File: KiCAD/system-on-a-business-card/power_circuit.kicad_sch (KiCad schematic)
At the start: 12 parts, among them U4 ZD1117ILTRAD

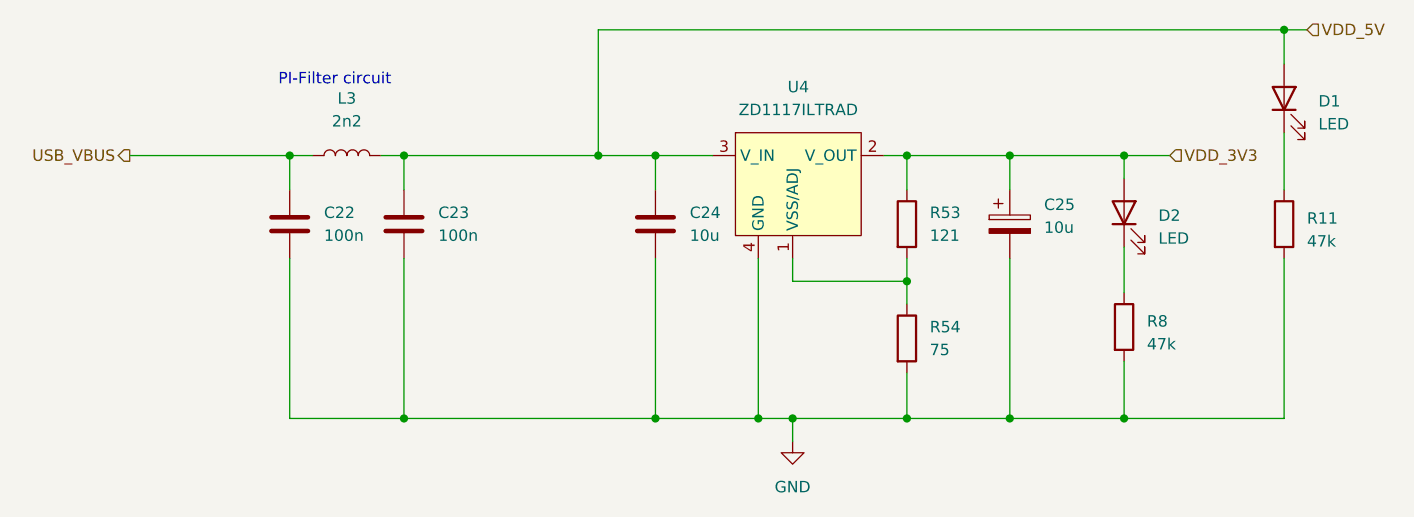
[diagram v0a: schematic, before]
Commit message: #10: mintor tweaks in routing, removed fiducials from bom, added values to buzzer and sd-card slot
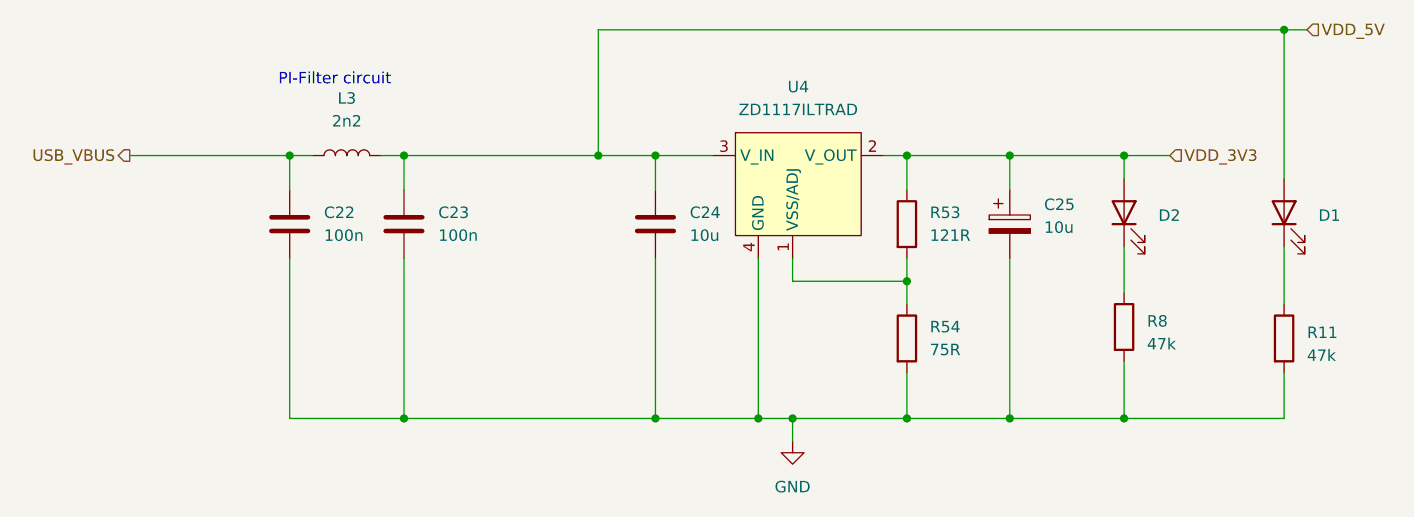
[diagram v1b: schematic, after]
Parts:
- D1, D2: value LED -> XL-1005UGC
- R53: value 121 -> 121R
- R54: value 75 -> 75R
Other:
- moved on the sheet: D1, R11
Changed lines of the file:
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@@
     (stroke (width 0) (type default))
   )
-  (wire (pts (xy 182.88 41.91) (xy 182.88 38.1))
+  (wire (pts (xy 182.88 54.61) (xy 182.88 38.1))
     (stroke (width 0) (type default))
   )
@@
     (stroke (width 0) (type default))
   )
-  (wire (pts (xy 182.88 63.5) (xy 182.88 81.28))
+  (wire (pts (xy 182.88 76.2) (xy 182.88 81.28))
     (stroke (width 0) (type default))
   )
@@
     (stroke (width 0) (type default))
   )
-  (wire (pts (xy 182.88 49.53) (xy 182.88 55.88))
+  (wire (pts (xy 182.88 62.23) (xy 182.88 68.58))
     (stroke (width 0) (type default))
   )
@@
     (effects (font (size 1.27 1.27)) (justify left))
   )
-  (symbol (lib_id "Device:LED") (at 182.88 45.72 90) (unit 1)
-    (in_bom yes) (on_board yes) (dnp no) (fields_autoplaced)
-    (property "Reference" "D1" (at 186.69 46.0374 90)
+  (symbol (lib_id "Device:LED") (at 182.88 58.42 90) (unit 1)
+    (in_bom yes) (on_board yes) (dnp no) (fields_autoplaced)
+    (property "Reference" "D1" (at 186.69 58.7374 90)
       (effects (font (size 1.27 1.27)) (justify right))
     )
-    (property "Value" "LED" (at 186.69 48.5774 90)
-      (effects (font (size 1.27 1.27)) (justify right))
-    )
-    (property "Footprint" "Diode_SMD:D_0402_1005Metric_Pad0.77x0.64mm_HandSolder" (at 182.88 45.72 0)
-      (effects (font (size 1.27 1.27)) hide)
-    )
-    (property "Datasheet" "~" (at 182.88 45.72 0)
+    (property "Value" "XL-1005UGC " (at 186.69 61.2774 90)
+      (effects (font (size 1.27 1.27)) (justify right) hide)
+    )
+    (property "Footprint" "Diode_SMD:D_0402_1005Metric_Pad0.77x0.64mm_HandSolder" (at 182.88 58.42 0)
+      (effects (font (size 1.27 1.27)) hide)
+    )
+    (property "Datasheet" "~" (at 182.88 58.42 0)
       (effects (font (size 1.27 1.27)) hide)
     )
@@
   (symbol (lib_id "Device:R") (at 140.97 72.39 0) (unit 1)
     (in_bom yes) (on_board yes) (dnp no) (fields_autoplaced)
-    (property "Reference" "R54" (at 143.51 71.1199 0)
-      (effects (font (size 1.27 1.27)) (justify left))
-    )
-    (property "Value" "75" (at 143.51 73.6599 0)
+    (property "Reference" "R54" (at 143.51 71.12 0)
+      (effects (font (size 1.27 1.27)) (justify left))
+    )
+    (property "Value" "75R" (at 143.51 73.66 0)
       (effects (font (size 1.27 1.27)) (justify left))
     )
@@
       (effects (font (size 1.27 1.27)) (justify right))
     )
-    (property "Value" "LED" (at 168.91 61.2774 90)
-      (effects (font (size 1.27 1.27)) (justify right))
+    (property "Value" "XL-1005UGC " (at 168.91 61.2774 90)
+      (effects (font (size 1.27 1.27)) (justify right) hide)
     )
     (property "Footprint" "Diode_SMD:D_0402_1005Metric_Pad0.77x0.64mm_HandSolder" (at 165.1 58.42 0)
@@
     )
   )
-  (symbol (lib_id "Device:R") (at 182.88 59.69 0) (unit 1)
-    (in_bom yes) (on_board yes) (dnp no) (fields_autoplaced)
-    (property "Reference" "R11" (at 185.42 59.055 0)
-      (effects (font (size 1.27 1.27)) (justify left))
-    )
-    (property "Value" "47k" (at 185.42 61.595 0)
-      (effects (font (size 1.27 1.27)) (justify left))
-    )
-    (property "Footprint" "Resistor_SMD:R_0402_1005Metric_Pad0.72x0.64mm_HandSolder" (at 181.102 59.69 90)
-      (effects (font (size 1.27 1.27)) hide)
-    )
-    (property "Datasheet" "~" (at 182.88 59.69 0)
+  (symbol (lib_id "Device:R") (at 182.88 72.39 0) (unit 1)
+    (in_bom yes) (on_board yes) (dnp no) (fields_autoplaced)
+    (property "Reference" "R11" (at 185.42 71.755 0)
+      (effects (font (size 1.27 1.27)) (justify left))
+    )
+    (property "Value" "47k" (at 185.42 74.295 0)
+      (effects (font (size 1.27 1.27)) (justify left))
+    )
+    (property "Footprint" "Resistor_SMD:R_0402_1005Metric_Pad0.72x0.64mm_HandSolder" (at 181.102 72.39 90)
+      (effects (font (size 1.27 1.27)) hide)
+    )
+    (property "Datasheet" "~" (at 182.88 72.39 0)
       (effects (font (size 1.27 1.27)) hide)
     )
@@
   (symbol (lib_id "Device:R") (at 140.97 59.69 0) (unit 1)
     (in_bom yes) (on_board yes) (dnp no) (fields_autoplaced)
-    (property "Reference" "R53" (at 143.51 58.4199 0)
-      (effects (font (size 1.27 1.27)) (justify left))
-    )
-    (property "Value" "121" (at 143.51 60.9599 0)
-      (effects (font (size 1.27 1.27)) (justify left))
-    )
+    (property "Reference" "R53" (at 143.51 58.42 0)
+      (effects (font (size 1.27 1.27)) (justify left))
+    )
+    (property "Value" "121R" (at 143.51 60.96 0)
+      (effects (font (size 1.27 1.27)) (justify left))
+    )
